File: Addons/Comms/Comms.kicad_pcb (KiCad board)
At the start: 2 copper layers, 33.5 x 31.2 mm, 12 parts, among them J1 Conn_01x02, J2 Conn_02x06_Odd_Even, J3 Conn_01x02, J4 Conn_01x01, U1 SP3485EN

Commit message: don't bridge 3v3 and ground lol
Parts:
- turned JP1 to 0 degrees
- turned JP2 to 180 degrees
- turned JP3 to 180 degrees
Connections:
- JP1 pad 1: GND -> Net-(JP1-A)
- JP1 pad 2: +3V3 -> Net-(JP1-B)
- JP2 pad 1: GND -> Net-(JP1-A)
- JP2 pad 2: Net-(JP2-B) -> GND
- JP3 pad 1: +3V3 -> Net-(JP1-B)
- JP3 pad 2: Net-(JP3-B) -> +3V3
- U1 pad 2: Net-(JP2-B) -> Net-(JP1-A)
- U1 pad 3: Net-(JP3-B) -> Net-(JP1-B)
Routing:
- net Net-(JP1-A): track 0.00 -> 31.0 mm, vias 0 -> 2
- net Net-(JP1-B): track 0.00 -> 21.4 mm, vias 0 -> 2
- net Net-(JP2-B): track 20.2 -> 0.00 mm, vias 2 -> 0
- net Net-(JP3-B): track 16.0 -> 0.00 mm, vias 2 -> 0
- net +3V3: track 47.6 -> 47.3 mm, vias 2 -> 3
- net GND: vias 2 -> 5
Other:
- board text added: "A"
- board text added: "B"

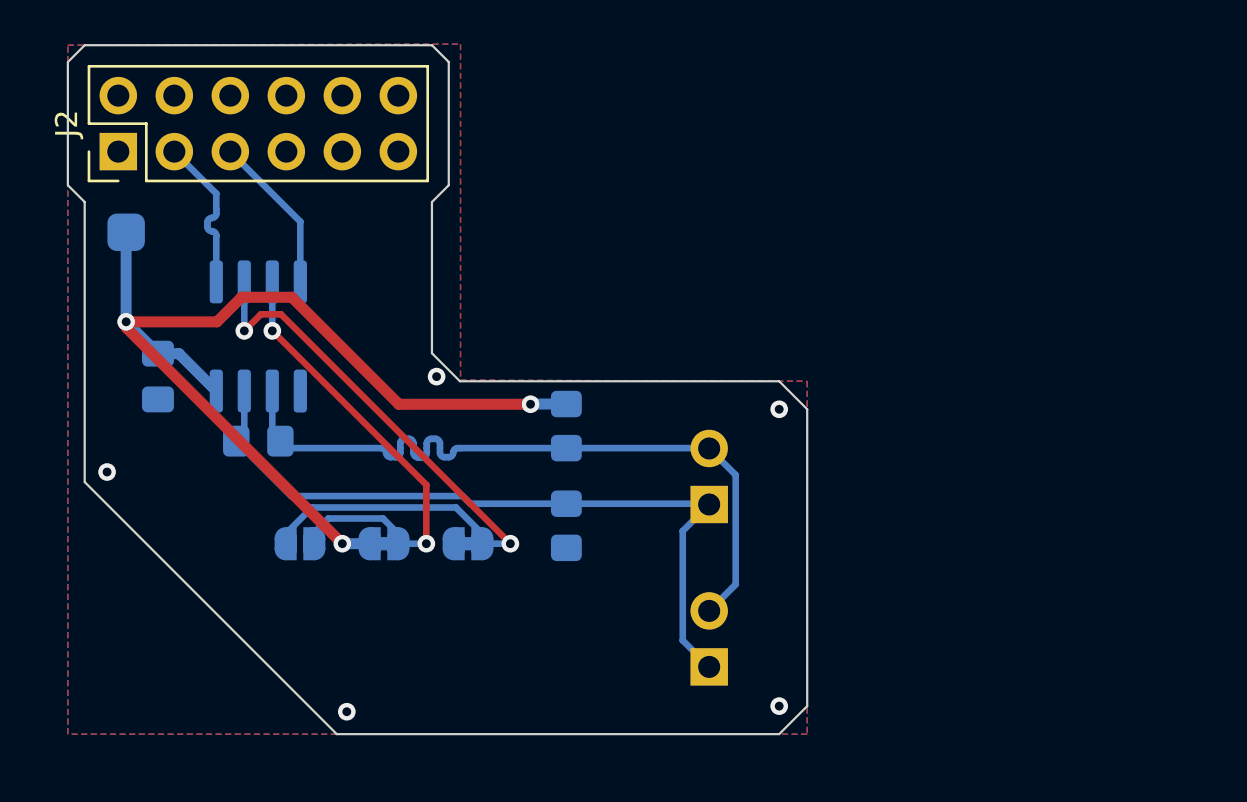
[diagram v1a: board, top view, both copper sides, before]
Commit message: Add RS485 functionality & addons, several fixes
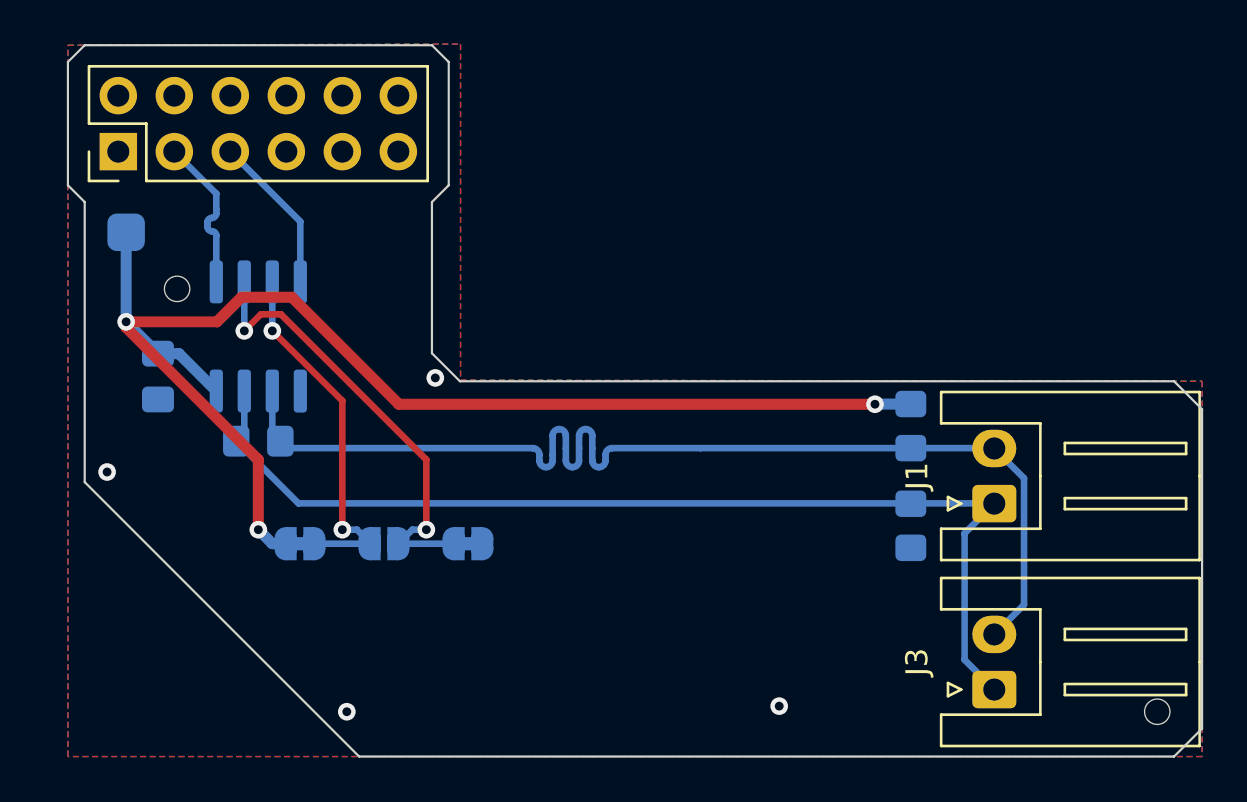
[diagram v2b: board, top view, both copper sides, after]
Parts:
- added REF**: ToolingHole_JLC, MountingHole:ToolingHole_JLC, F.Cu at (105.5, 50.8)
- added REF**: ToolingHole_JLC, MountingHole:ToolingHole_JLC, F.Cu at (61.1, 31.6)
- J1, J3: footprint Connector_PinHeader_2.54mm:PinHeader_1x02_P2.54mm_Horizontal -> Connector_JST:JST_XH_S2B-XH-A_1x02_P2.50mm_Horizontal; moved to F.Cu
- moved R3 15.6 mm to (94.4, 37.8)
- moved R5 15.6 mm to (94.4, 42.4)
- moved J3 15.4 mm to (98.1, 49.8), turned to 90 degrees
- moved J1 14.9 mm to (98.1, 41.4), turned to 90 degrees
- moved JP1 3.81 mm to (70.5, 43.2), turned to 180 degrees
- moved JP3 3.81 mm to (66.7, 43.2)
- turned JP2 to 0 degrees
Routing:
- net /RS485_A: track 33.4 -> 51.4 mm
- net /RS485_B: track 33.4 -> 47.5 mm
- net +3V3: track 47.3 -> 60.9 mm
- net Net-(JP1-A): track 31.0 -> 20.7 mm
- net Net-(JP1-B): track 21.4 -> 16.6 mm
- net GND: vias 5 -> 4
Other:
- board size 33.5 x 31.2 mm -> 51.4 x 32.3 mm
- board text added: "CUT RE/DE JUMPERS TO SWITCH RE/DE MANUALLY WITH WIRE TO GP1"
- board text removed: "CUT RE/DE JUMPERS TO SWITCH RE/DE MANYALLY WITH WIRE TO GP1"
